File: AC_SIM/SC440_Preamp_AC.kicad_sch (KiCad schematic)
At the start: 22 parts, among them J1 ANALOG BOARD, J2 JST-XH 1x04 TO DIGITAL BOARD, U1 OPA1678IDR

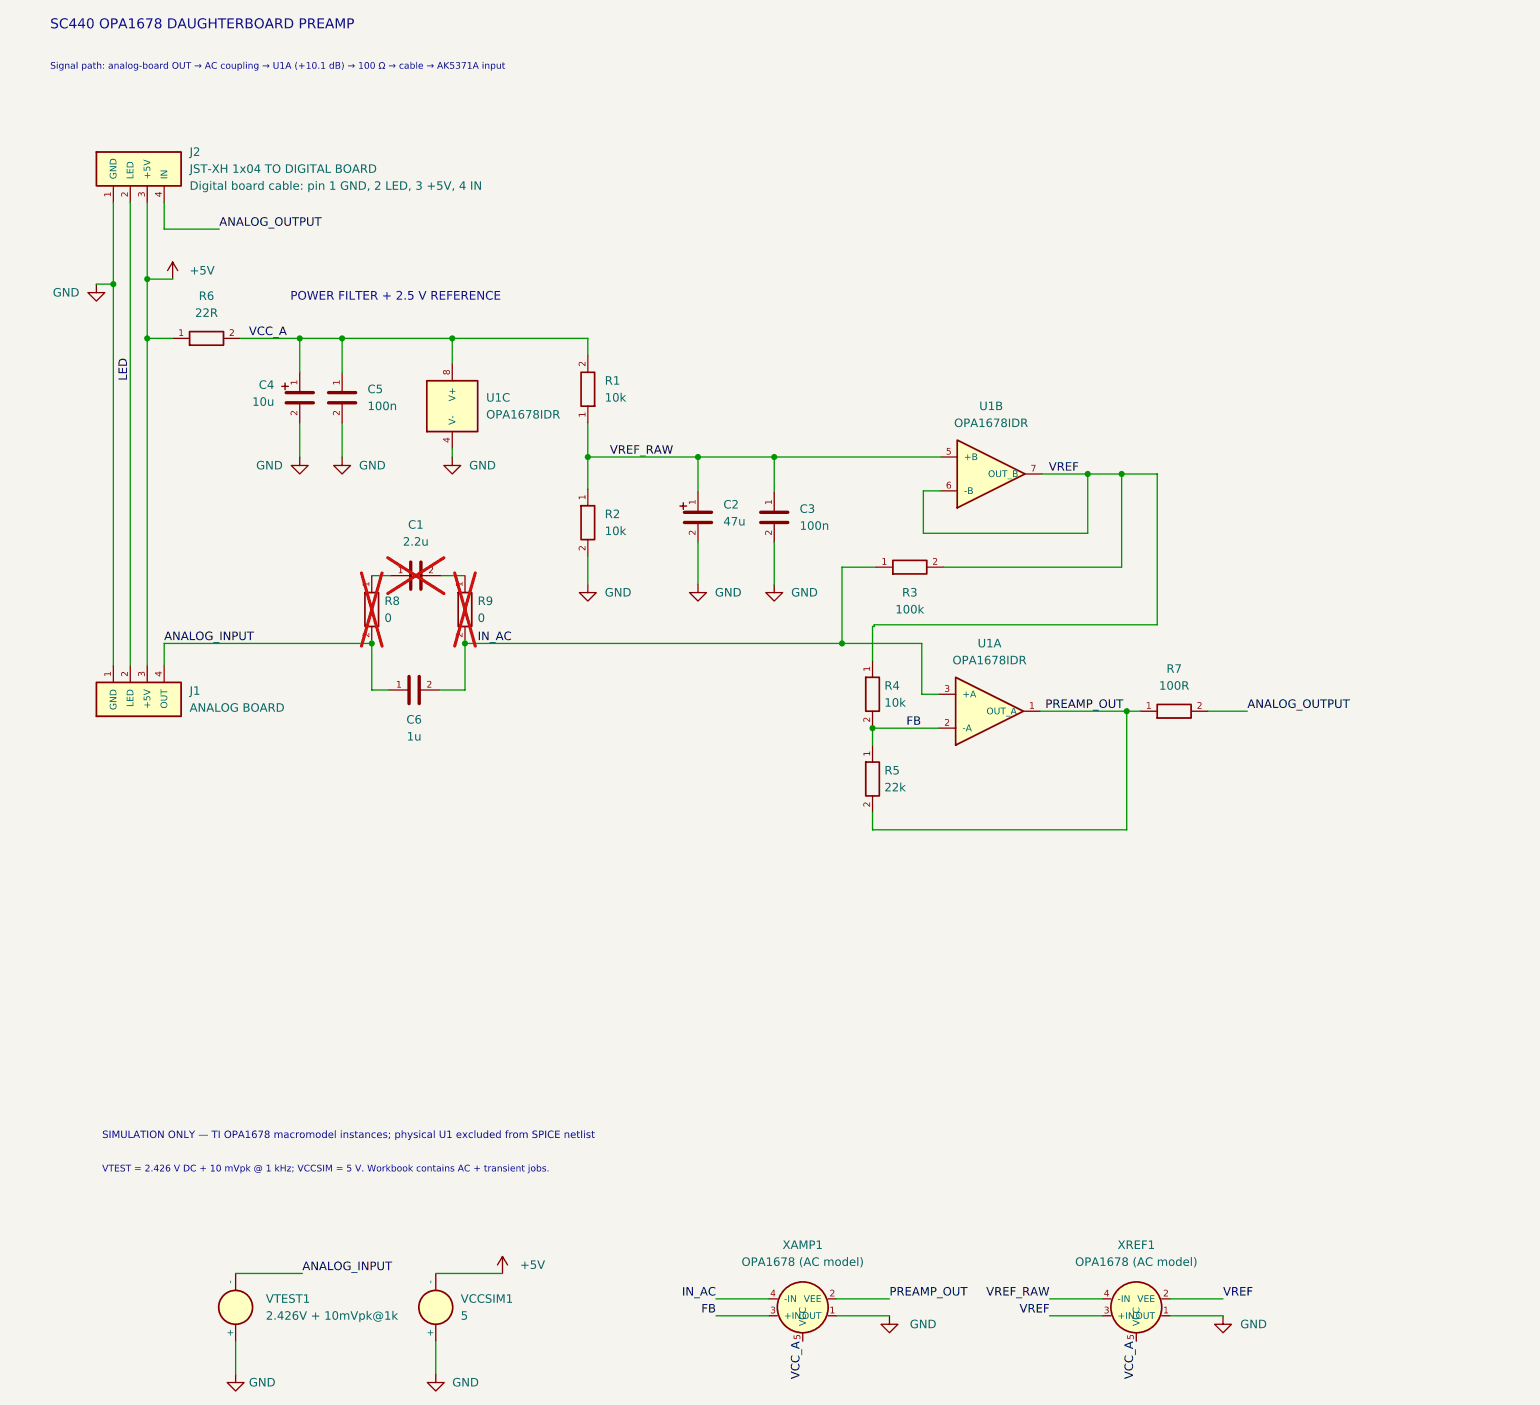
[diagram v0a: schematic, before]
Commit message: docs: update BOM and assembly variants; sync and fix simulations
- Document current hardware, MLCC/film options and 6/8/10 dB variants
- Synchronize AC project and reference netlists with current schematic
- Include C4/C8 in BOM and exclude test points from SPICE export
- Validate connectivity and all six AC assembly variants
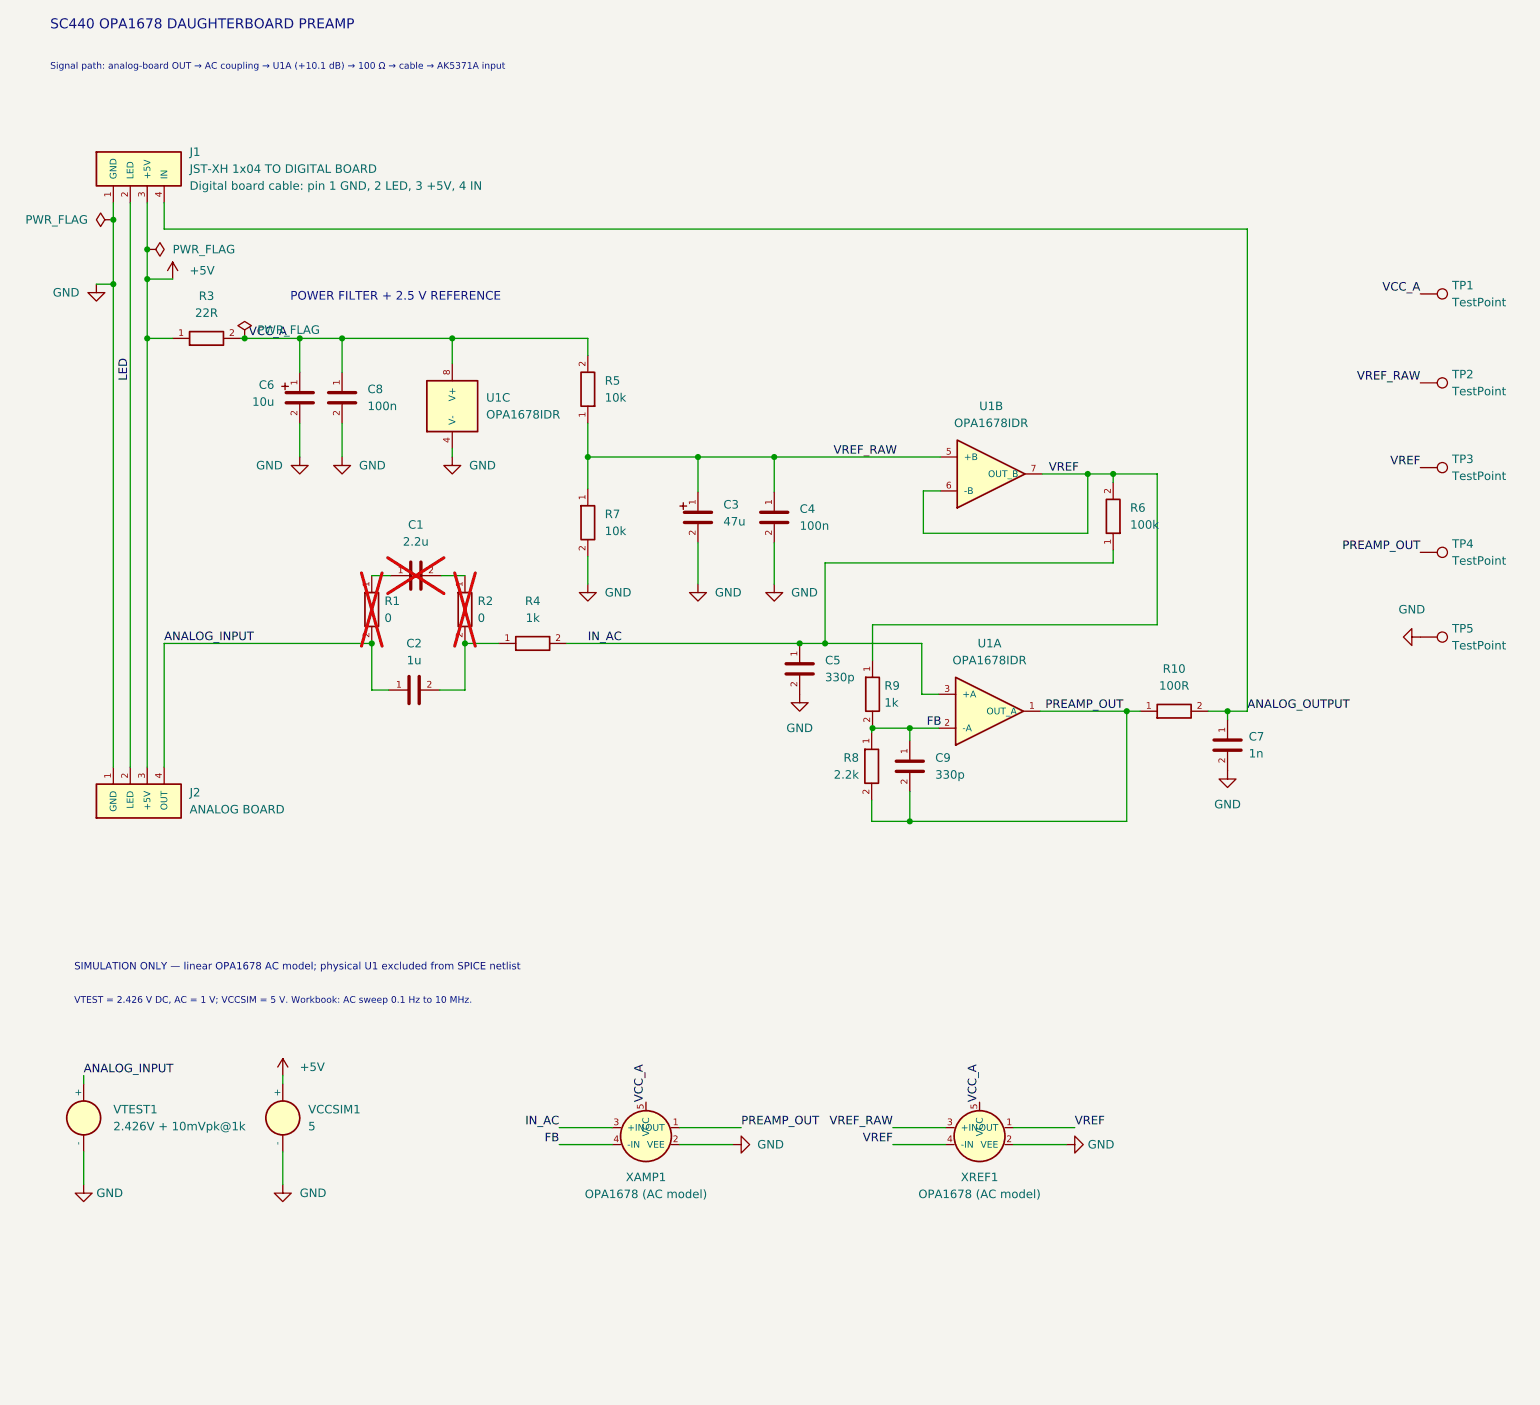
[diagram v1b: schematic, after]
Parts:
- removed R3: 100k, Resistor_SMD:R_0805_2012Metric_Pad1.20x1.40mm_HandSolder, symbol SC440_Preamp:R
- removed R5: 22k, Resistor_SMD:R_0805_2012Metric_Pad1.20x1.40mm_HandSolder, symbol SC440_Preamp:R
- added C5, C9: 330p, Capacitor_SMD:C_0805_2012Metric_Pad1.18x1.45mm_HandSolder, symbol SC440_Preamp:C
- added C7: 1n, Capacitor_SMD:C_0805_2012Metric_Pad1.18x1.45mm_HandSolder, symbol SC440_Preamp:C
- added R4: 1k, Resistor_SMD:R_0805_2012Metric_Pad1.20x1.40mm_HandSolder, symbol SC440_Preamp:R
- added R6: 100k, Resistor_SMD:R_0805_2012Metric_Pad1.20x1.40mm_HandSolder, symbol SC440_Preamp:R
- added R8: 2.2k, Resistor_SMD:R_0805_2012Metric_Pad1.20x1.40mm_HandSolder, symbol SC440_Preamp:R
- added TP1, TP2, TP3, TP4, TP5: TestPoint, TestPoint:TestPoint_THTPad_1.0x1.0mm_Drill0.5mm, symbol Connector:TestPoint
- C2: renamed from C6; KiLib_Generator (none) -> SMD_2terminal_chip_molded
- C3: renamed from C2; KiLib_Generator (none) -> capacitor/THT/other
- C4: renamed from C3; KiLib_Generator (none) -> SMD_2terminal_chip_molded
- C6: renamed from C4; KiLib_Generator (none) -> capacitor/THT/other
- C8: renamed from C5; KiLib_Generator (none) -> SMD_2terminal_chip_molded
- J1: renamed from J2; KiLib_Generator (none) -> connector/JST
- J2: renamed from J1; KiLib_Generator (none) -> connector/pin_header_socket
- R1: renamed from R8; KiLib_Generator (none) -> SMD_2terminal_chip_molded
- R10: renamed from R7; KiLib_Generator (none) -> SMD_2terminal_chip_molded
- R2: renamed from R9; KiLib_Generator (none) -> SMD_2terminal_chip_molded
- R3: renamed from R6; KiLib_Generator (none) -> SMD_2terminal_chip_molded
- R5: renamed from R1; KiLib_Generator (none) -> SMD_2terminal_chip_molded
- R7: renamed from R2; KiLib_Generator (none) -> SMD_2terminal_chip_molded
- R9: renamed from R4; value 10k -> 1k; KiLib_Generator (none) -> SMD_2terminal_chip_molded
- U1: KiLib_Generator (none) -> package/gullwing
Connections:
- net +5V: now also VCCSIM1.1 (+); no longer VCCSIM1.2 (-)
- net ANALOG_INPUT: now also VTEST1.1 (+); no longer VTEST1.2 (-)
- net ANALOG_OUTPUT: now also C7.1
- net FB: now also XAMP1.4 (-IN), C9.1, R8.1; no longer XAMP1.3 (+IN)
- net GND: now also VCCSIM1.2 (-), VTEST1.2 (-), XAMP1.2 (VEE), XREF1.2 (VEE), C5.2, C7.2, TP5.1; no longer VCCSIM1.1 (+), VTEST1.1 (+), XAMP1.1 (OUT), XREF1.1 (OUT)
- net IN_AC: now also XAMP1.3 (+IN), C5.1, R4.2, R6.1; no longer C2.2, R2.2, XAMP1.4 (-IN)
- net PREAMP_OUT: now also XAMP1.1 (OUT), C9.2, R8.2, TP4.1; no longer XAMP1.2 (VEE)
- net VCC_A: now also TP1.1
- net VREF: now also XREF1.1 (OUT), XREF1.4 (-IN), R6.2, TP3.1; no longer XREF1.2 (VEE), XREF1.3 (+IN)
- net VREF_RAW: now also XREF1.3 (+IN), TP2.1; no longer XREF1.4 (-IN)
- new net: C2.2, R2.2, R4.1
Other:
- note added: "SIMULATION ONLY — linear OPA1678 AC model; physical U1 excluded from SPICE netlist"
- note added: "VTEST = 2.426 V DC, AC = 1 V; VCCSIM = 5 V. Workbook: AC sweep 0.1 Hz to 10 MHz."
- note removed: "SIMULATION ONLY — TI OPA1678 macromodel instances; physical U1 excluded from SPICE netlist"
- note removed: "VTEST = 2.426 V DC + 10 mVpk @ 1 kHz; VCCSIM = 5 V. Workbook contains AC + transient jobs."
- moved on the sheet: J2, XAMP1, XREF1
